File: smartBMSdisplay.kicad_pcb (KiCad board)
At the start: 2 copper layers, 95.9 x 45.1 mm, 11 parts, among them J1 Conn_01x04_Male, J2 Conn_01x05_Male, Q1 BC547

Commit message: First working bluetooth version
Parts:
- removed A1: Arduino_Nano_v2.x, Module:Arduino_Nano
- added U1: esp32_WROOM, ESP32-smartBMSdisplay:ESP32_Devkit_38Pins, F.Cu at (149.9, 73.0)
- moved H4 7.43 mm to (191.8, 98.4)
- moved H2 7.01 mm to (108.0, 98.4)
- moved Brd1 5.43 mm to (171.4, 82.5)
- moved H3 3.59 mm to (191.8, 66.7)
- moved H1 3.24 mm to (108.0, 66.7)
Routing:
- net GND: track 104.3 -> 84.6 mm, vias 0 -> 1
- net Net-(Brd1-Pad3): track 52.3 -> 33.1 mm
- net Net-(Brd1-Pad4): track 48.7 -> 35.6 mm
- net Net-(R1-Pad2): track 27.5 -> 40.0 mm
- net Net-(Brd1-Pad7): track 37.9 -> 46.4 mm
- net Net-(J1-Pad3): track 49.1 -> 55.2 mm
- net Net-(Brd1-Pad5): track 45.1 -> 39.2 mm
- net Net-(J1-Pad2): track 57.0 -> 52.1 mm, vias 0 -> 1
- net Net-(B1-Pad1): track 54.1 -> 57.0 mm
- net Net-(Brd1-Pad6): track 41.5 -> 42.8 mm
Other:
- board size 95.9 x 45.1 mm -> 95.3 x 50.8 mm
- board text removed: "1"
- board text removed: "15"
- board text removed: "16"
- board text removed: "30"
- board text removed: "Arduino Nano 2"
- board text removed: "SSD 1309 128x64 2.52{dblquote} SPI Interface"

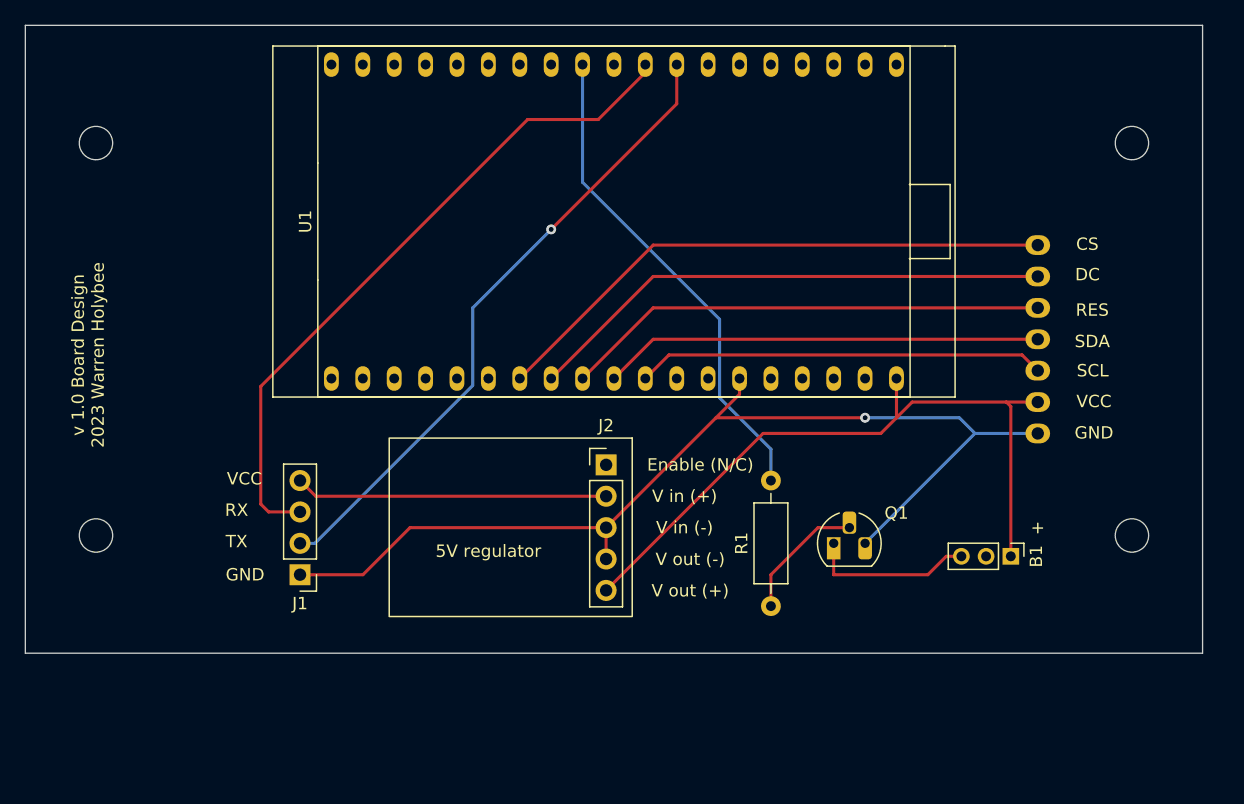
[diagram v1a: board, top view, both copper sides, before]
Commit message: Update Readme, misc display changes, update PCB
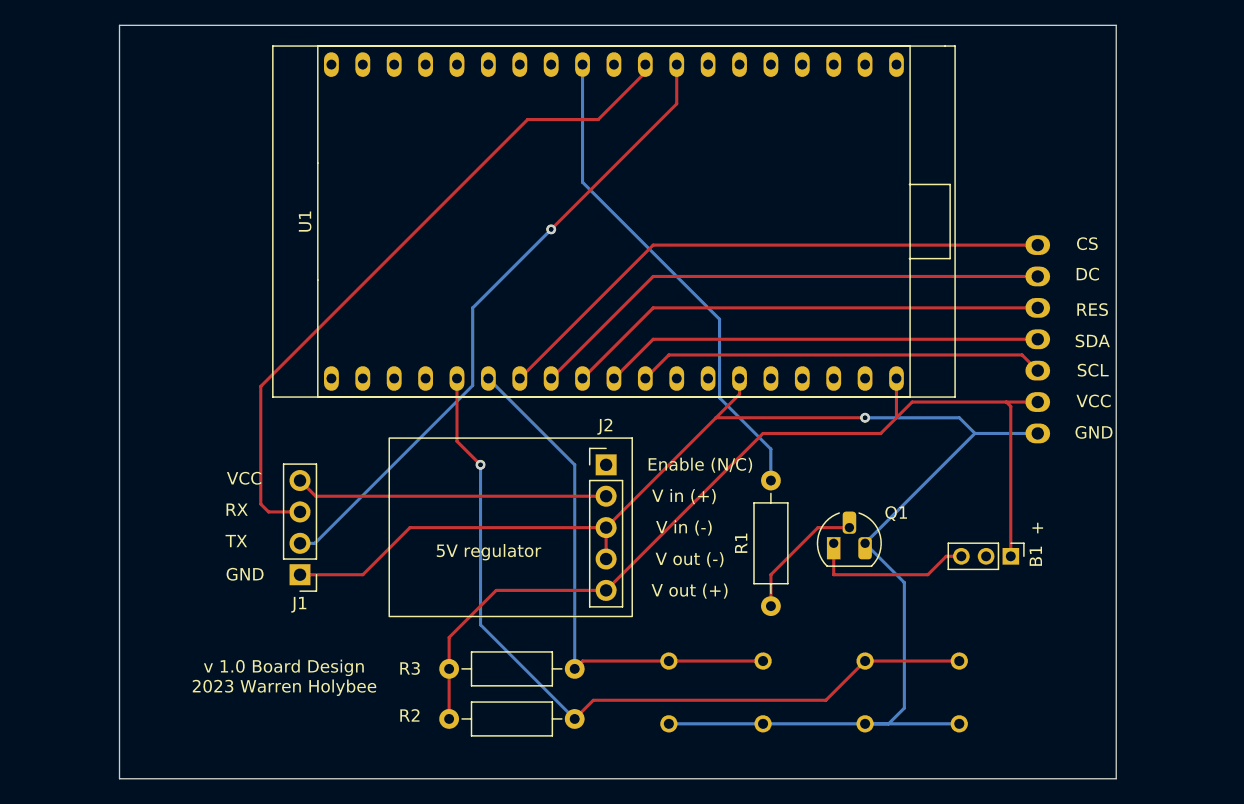
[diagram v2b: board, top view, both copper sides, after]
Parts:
- removed H1, H2, H3, H4: MountingHole_2.7mm_M2.5, MountingHole:MountingHole_2.7mm_M2.5
- added R2: 10k, Resistor_THT:R_Axial_DIN0207_L6.3mm_D2.5mm_P10.16mm_Horizontal, F.Cu at (136.5, 113.3)
- added R3: 10k, Resistor_THT:R_Axial_DIN0207_L6.3mm_D2.5mm_P10.16mm_Horizontal, F.Cu at (136.5, 109.2)
- added SW1: Switch_1, Button_Switch_THT:SW_Tactile_Straight_KSA0Axx1LFTR, B.Cu at (177.8, 108.6)
- added SW2: Switch_2, Button_Switch_THT:SW_Tactile_Straight_KSA0Axx1LFTR, B.Cu at (161.9, 108.6)
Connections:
- U1 pad 5: unconnected-(U1-Pad5) -> Net-(R2-Pad2)
- U1 pad 6: unconnected-(U1-Pad6) -> Net-(SW2-Pad1)
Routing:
- net Net-(R2-Pad2): track 0.00 -> 64.5 mm, vias 0 -> 1
- net Net-(SW2-Pad1): track 0.00 -> 41.9 mm
- net GND: track 84.6 -> 126.4 mm
- net Net-(B1-Pad1): track 57.0 -> 77.9 mm
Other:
- board size 95.3 x 50.8 mm -> 80.6 x 61 mm
- board text removed: "Arduino Xiaoxiang Smart BMS Display https://github.com/vagueDirector/ArduinoXiaoxiangSmartBMSDisplay"
